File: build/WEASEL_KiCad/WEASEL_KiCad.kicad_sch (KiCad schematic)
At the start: 104 parts, among them J1 MIDI IN, J10 LPG_LEVEL2CTRL, J14 SEQ_OUTPUT2, J15 SEQ_OUTPUT3, J16 EG_OUTPUT1, J17 EG_OUTPUT2, J18 EG_OUTPUT3, J19 PLSR_OUTPUT1, J2 STEREO_OUTPUT, J20 PLSR_OUTPUT2, J21 PLSR_OUTPUT3, J22 RNDM_OUTPUT1, J23 RNDM_OUTPUT2, J24 RNDM_OUTPUT3, J3 SEQ_OUTPUT1, J4 PLSR_PERIODCTRL, J5 MODOSC_FREQCTRL, J6 MODOSC_MODCTRL, J7 COMPOSC_PITCHCTRL, J8 COMPOSC_WAVEFOLDERCTRL, J9 LPG_LEVEL1CTRL, SW1 SQ_TOGGLESTEP1, SW2 SEQ_TRIGGERSELECT, SW3 SQ_TOGGLESTEP2, SW31 EG_TRIGGERSELECT, SW32 EG_MODESELECT, SW33 PLSR_TRIGGERSELECT, SW34 PLSR_MODE, SW35 MODOSC_MIDITOGGLE, SW36 MODOSC_PITCHTRANGE, SW37 COMPLEXOSC_MIDITOGGLE, SW38 COMPLEXOSC_POLARITY, SW39 COMPLEXOSC_WAVETOGGLE, SW4 SQ_TOGGLESTEP3, SW40 LPG_GATE1MODE, SW41 LPG_GATE2MODE, SW42 RNDMVOLTAGE_TRIGGERSELECT, SW43 CLOCK_SYNCTOGGLE, SW5 SQ_TOGGLESTEP4, SW6 SEQ_STAGES, SW7 SQ_TOGGLESTEP5, U1 CD74HC4067, U2 CD74HC4067, U3 6N138

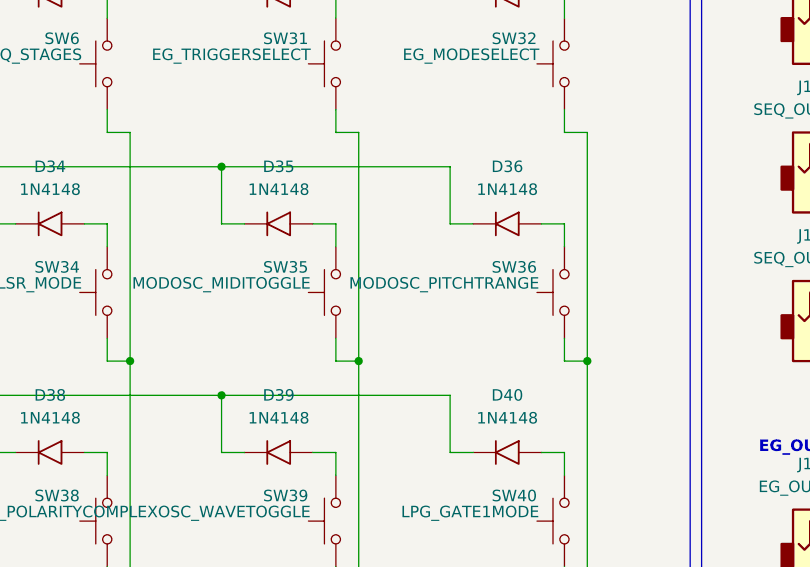
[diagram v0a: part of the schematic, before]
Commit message: FW update - prototype board
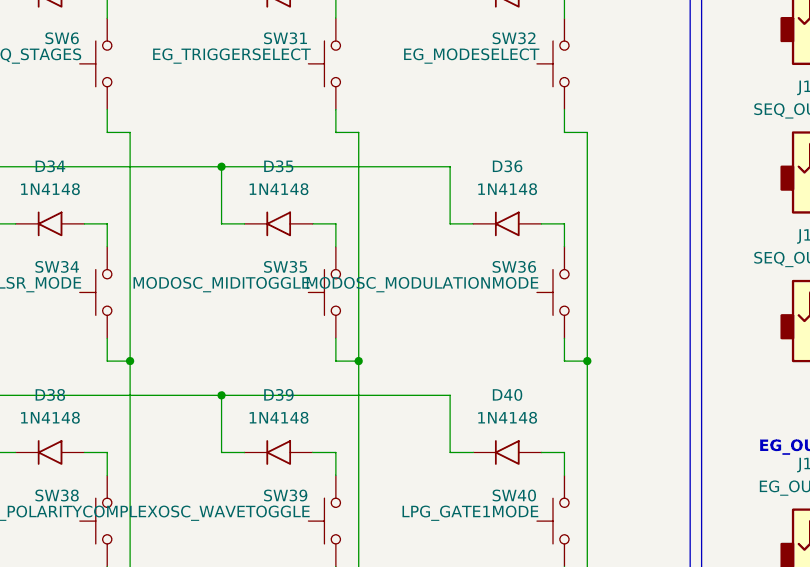
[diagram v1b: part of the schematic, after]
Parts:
- SW36: value MODOSC_PITCHTRANGE -> MODOSC_MODULATIONMODE
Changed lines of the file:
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@@
 			)
 		)
-		(property "Value" "MODOSC_PITCHTRANGE"
+		(property "Value" "MODOSC_MODULATIONMODE"
 			(at 138.176 211.074 90)
 			(effects

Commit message: PCB V2.0
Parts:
- J1, J2: footprint Connector_Audio:Jack_3.5mm_CUI_SJ1-3523N_Horizontal -> trsSocket:Jack_3.5mm_CUI_SJ1-3523N_Horizontal_edited_noEdgeCuts
- RV1, RV10, RV11, RV12, RV13, RV14, RV16, RV17, RV19, RV2, RV20, RV22, RV23, RV24, RV25, RV3, RV4, RV5, RV6, RV7, RV8, RV9: footprint DIYSynthMNL:Potentiometer_RV09_BigPads -> Potentiometer_THT:Potentiometer_Bourns_PTA2043_Single_Slide
- U1, U2: footprint CD74HC4067 MUX:CD74HC4067 -> CD74HC4067 MUX:CD74HC4067_matchesSymbol
- renumbered D44 to D1, D36 to D10, D37 to D11, D38 to D12, D39 to D13, D40 to D14, D41 to D15, D42 to D16, D43 to D17, D45 to D18, D46 to D19, D47 to D20, D48 to D21, D49 to D22, D1 to D23, D2 to D24, D3 to D25, D4 to D26, D6 to D27, D7 to D28, D8 to D29, D5 to D3, D30 to D4, D31 to D5, D32 to D6, D33 to D7, D34 to D8, D35 to D9, J20 to J10, J21 to J11, J22 to J12, J23 to J13, J24 to J14, J4 to J15, J5 to J16, J6 to J17, J7 to J18, J8 to J19, J9 to J20, J10 to J21, J14 to J4, J15 to J5, J16 to J6, J17 to J7, J18 to J8, J19 to J9, R10 to R1, R9 to R2, SW2 to SW1, SW38 to SW10, SW39 to SW11, SW40 to SW12, SW41 to SW13, SW42 to SW14, SW43 to SW15, SW1 to SW16, SW3 to SW17, SW4 to SW18, SW5 to SW19, SW6 to SW2, SW7 to SW20, SW31 to SW3, SW32 to SW4, SW33 to SW5, SW34 to SW6, SW35 to SW7, SW36 to SW8, SW37 to SW9
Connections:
- net GND: now also RV12.1; no longer A1.20 (AGND), J2.S, RV12.3
- net Vcc: now also RV12.3; no longer RV12.1
- new net AGND: A1.20 (AGND), J2.S
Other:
- moved on the sheet: RV12

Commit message: PCB & UI 2.0
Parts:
- SW7: value MODOSC_MIDITOGGLE -> MODOSC_WAVEFORMTOGGLE
- SW9: value COMPLEXOSC_MIDITOGGLE -> OSCILLATOR_MIDITOGGLE
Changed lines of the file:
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@@
 			)
 		)
-		(property "Value" "MODOSC_MIDITOGGLE"
+		(property "Value" "MODOSC_WAVEFORMTOGGLE"
 			(at 112.776 211.074 90)
 			(effects
@@
 			)
 		)
-		(property "Value" "COMPLEXOSC_MIDITOGGLE"
+		(property "Value" "OSCILLATOR_MIDITOGGLE"
 			(at 61.468 236.982 90)
 			(effects

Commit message: PCB & UI 2.0
Front Panel final
Back panel Final
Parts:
- SW7: value MODOSC_WAVEFORMTOGGLE -> MODOSC_MODULATIONMODE
- SW8: value MODOSC_MODULATIONMODE -> MODOSC_WAVEFORMTOGGLE
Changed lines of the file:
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@@
 			)
 		)
-		(property "Value" "MODOSC_WAVEFORMTOGGLE"
-			(at 112.776 211.074 90)
+		(property "Value" "MODOSC_MODULATIONMODE"
+			(at 119.126 216.408 90)
 			(effects
 				(font
@@
 			)
 		)
-		(property "Value" "MODOSC_MODULATIONMODE"
-			(at 138.176 211.074 90)
+		(property "Value" "MODOSC_WAVEFORMTOGGLE"
+			(at 142.24 207.772 90)
 			(effects
 				(font

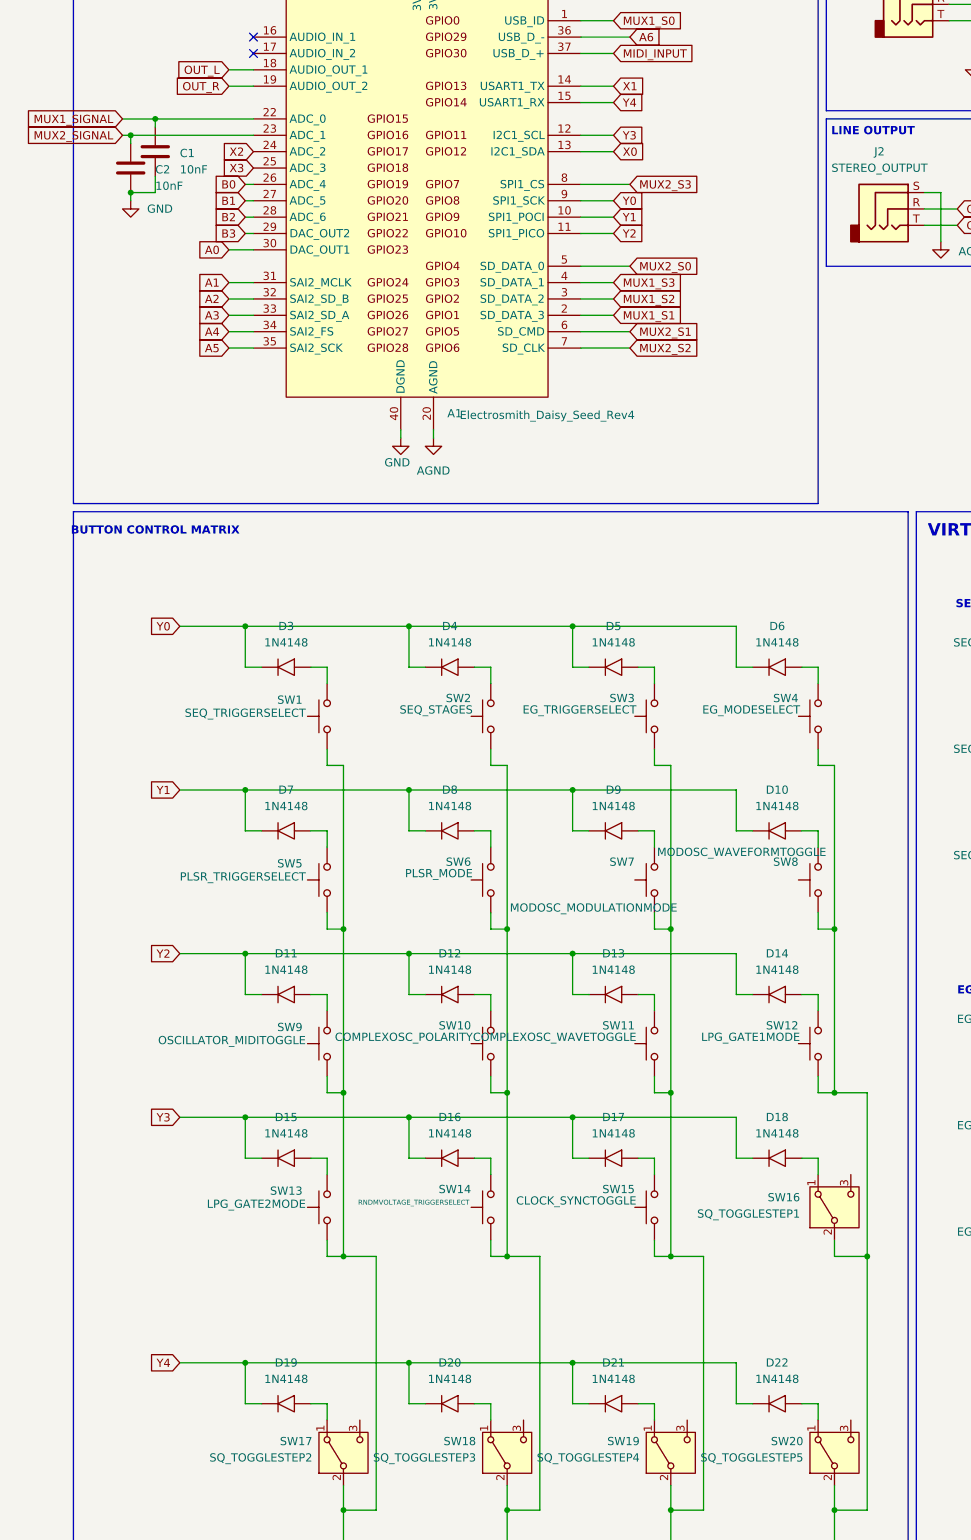
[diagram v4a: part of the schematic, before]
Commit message: PCB and Firmware Updates
- Updated PCBs
- Updated firmware to add sequencer trigger toggle - sequencer can now be triggered by pulser. Midi is WIP
- Updated Pot names in Serial
- Fixed X1 Row button issues
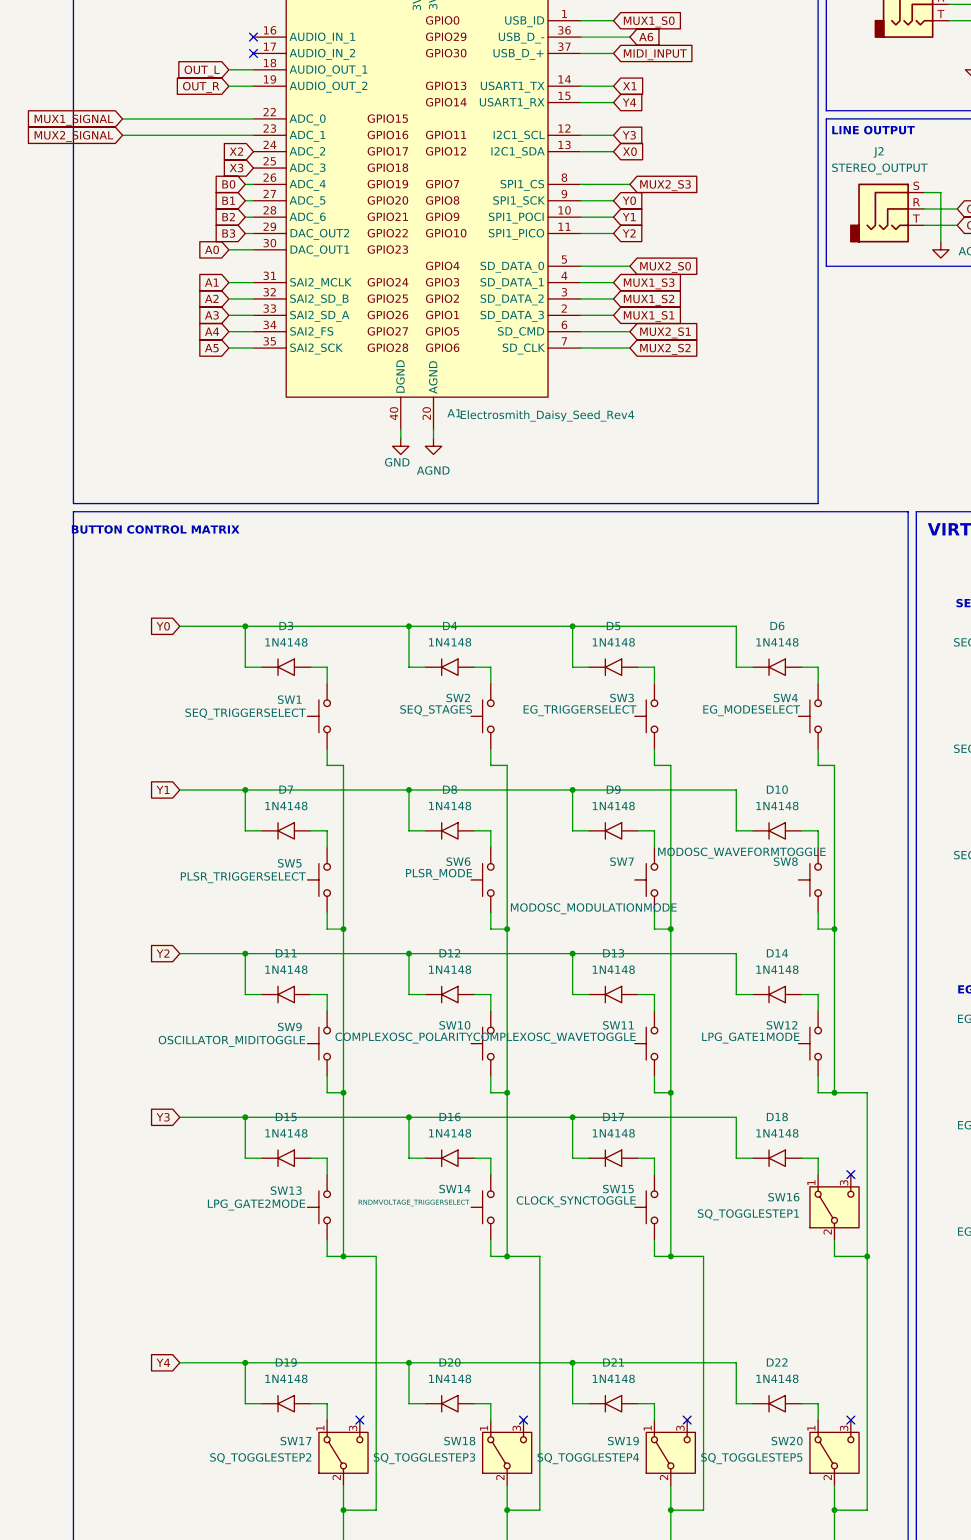
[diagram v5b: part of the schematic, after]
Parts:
- removed C1, C2: 10nF, PCM_4ms_Capacitor:C_Disc_P5.08mm, symbol Device:C
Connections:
- no-connect marks 9 -> 14

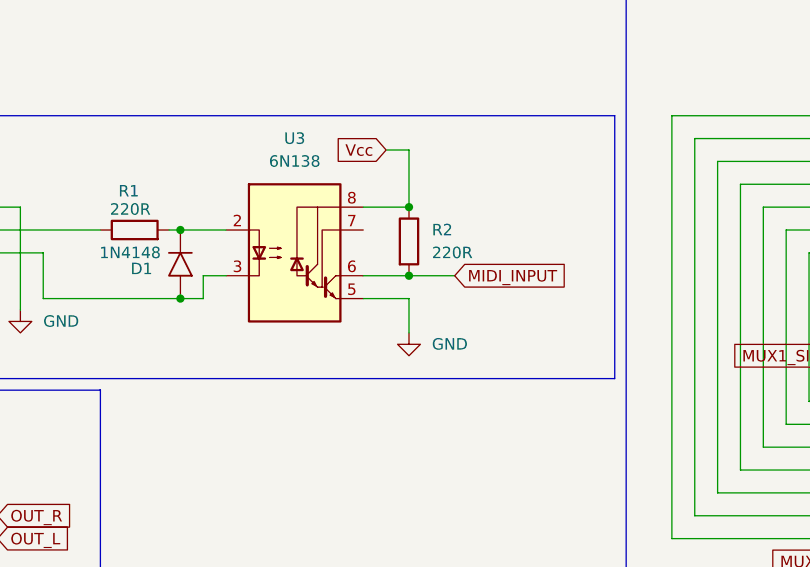
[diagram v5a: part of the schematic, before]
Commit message: Smoothed POTS
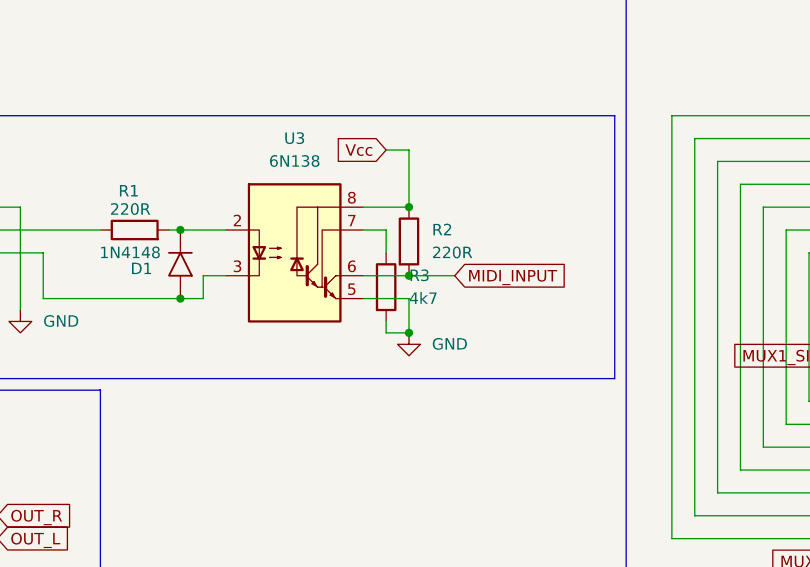
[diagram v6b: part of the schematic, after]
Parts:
- added R3: 4k7, PCM_4ms_Resistor:R_Axial_DIN0207_L6.3mm_D2.5mm_P7.62mm_Horizontal, symbol Device:R
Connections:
- net GND: now also R3.2
- net at U3.7 (VO1): now also R3.1
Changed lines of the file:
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@@
 	)
 	(junction
+		(at 208.28 87.63)
+		(diameter 0)
+		(color 0 0 0 0)
+	)
+	(junction
 		(at 205.74 270.51)
 		(diameter 0)
@@
 	(wire
 		(pts
+			(xy 205.74 87.63) (xy 208.28 87.63)
+		)
+		(stroke
+			(width 0)
+			(type default)
+		)
+	)
+	(wire
+		(pts
 			(xy 568.96 172.72) (xy 568.96 198.12)
 		)
@@
 	(wire
 		(pts
+			(xy 205.74 76.2) (xy 203.2 76.2)
+		)
+		(stroke
+			(width 0)
+			(type default)
+		)
+	)
+	(wire
+		(pts
 			(xy 238.76 179.07) (xy 246.38 179.07)
 		)
@@
 	(wire
 		(pts
+			(xy 205.74 78.74) (xy 205.74 76.2)
+		)
+		(stroke
+			(width 0)
+			(type default)
+		)
+	)
+	(wire
+		(pts
 			(xy 238.76 207.01) (xy 238.76 209.55)
 		)
@@
 	(wire
 		(pts
+			(xy 205.74 86.36) (xy 205.74 87.63)
+		)
+		(stroke
+			(width 0)
+			(type default)
+		)
+	)
+	(wire
+		(pts
 			(xy 321.31 101.6) (xy 706.12 101.6)
 		)
@@
 					(unit 1)
 				)
+			)
+		)
+	)
+	(symbol
+		(lib_id "Device:R")
+		(at 205.74 82.55 0)
+		(unit 1)
+		(exclude_from_sim no)
+		(in_bom yes)
+		(on_board yes)
+		(dnp no)
+		(property "Reference" "R3"
+			(at 208.28 81.2799 0)
+			(effects
+				(font
+					(size 1.27 1.27)
+				)
+				(justify left)
+			)
+		)
+		(property "Value" "4k7"
+			(at 208.28 83.8199 0)
+			(effects
+				(font
+					(size 1.27 1.27)
+				)
+				(justify left)
+			)
+		)
+		(property "Footprint" "PCM_4ms_Resistor:R_Axial_DIN0207_L6.3mm_D2.5mm_P7.62mm_Horizontal"
+			(at 203.962 82.55 90)
+			(effects
+				(font
+					(size 1.27 1.27)
+				)
+				(hide yes)
+			)
+		)
+		(property "Datasheet" "~"
+			(at 205.74 82.55 0)
+			(effects
+				(font
+					(size 1.27 1.27)
+				)
+				(hide yes)
+			)
+		)
+		(property "Description" "Resistor"
+			(at 205.74 82.55 0)
+			(effects
+				(font
+					(size 1.27 1.27)
+				)
+				(hide yes)
+			)
+		)
+		(pin "1"
+		)
+		(pin "2"
+		)
+		(instances
+			(project "WEASEL_KiCad"
+				(path "/3720ecea-634e-451d-a5f4-988a924d60a3"
+					(reference "R3")
+					(unit 1)
+				)

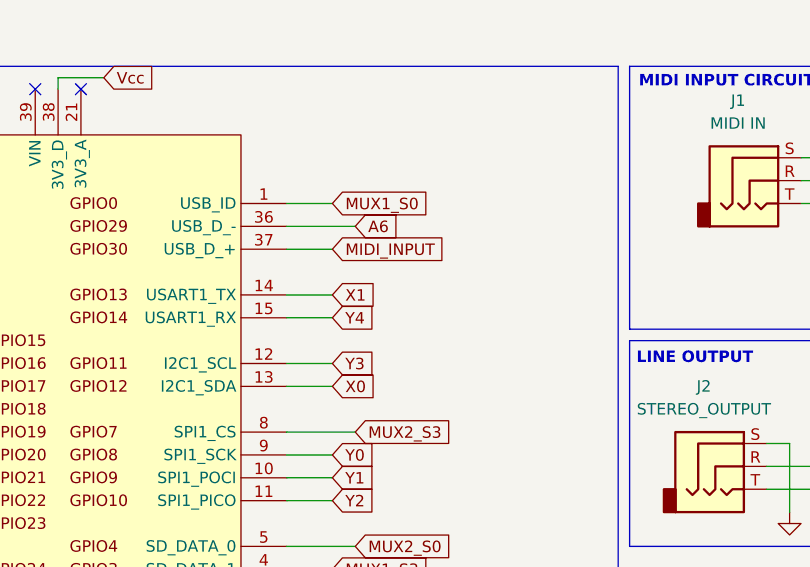
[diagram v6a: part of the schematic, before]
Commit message: MIDI IN pots change
Swapped Y4 and RX pins
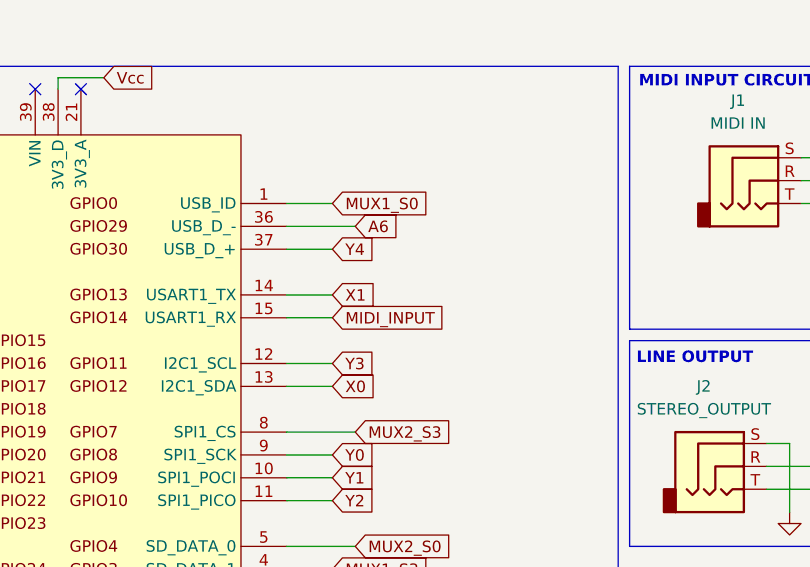
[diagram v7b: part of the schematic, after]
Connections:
- net MIDI_INPUT: now also A1.15 (USART1_RX); no longer A1.37 (USB_D_+)
- net Y4: now also A1.37 (USB_D_+); no longer A1.15 (USART1_RX)

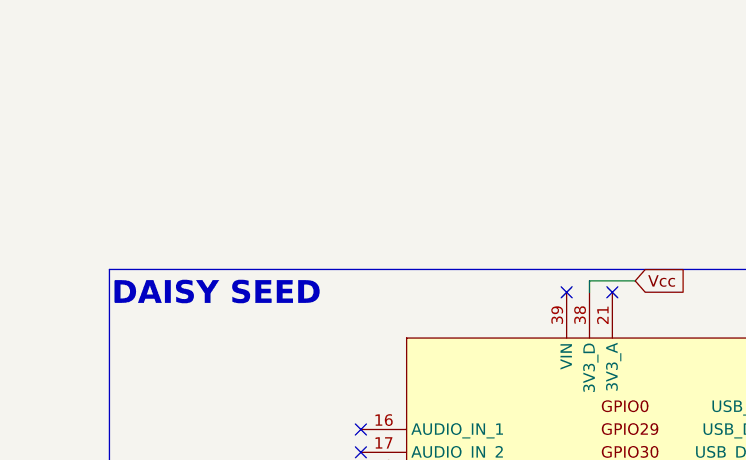
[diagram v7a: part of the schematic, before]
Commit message: PCB Update
Added  5V Power Input
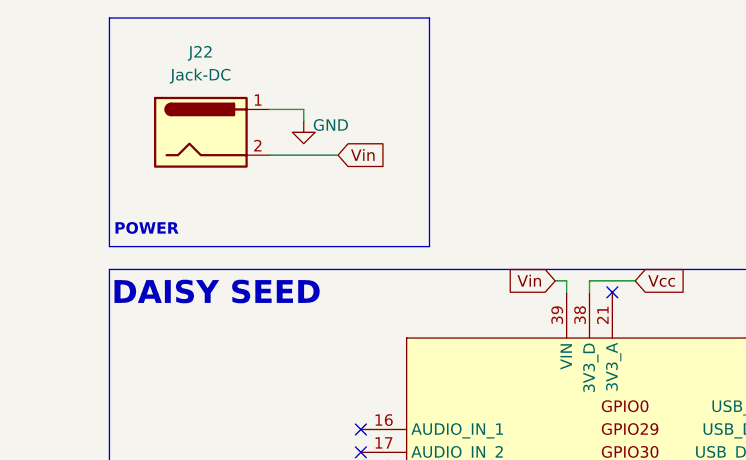
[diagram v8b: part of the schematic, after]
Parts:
- added J22: Jack-DC, Connector_BarrelJack:BarrelJack_GCT_DCJ200-10-A_Horizontal, symbol Connector:Jack-DC
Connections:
- net GND: now also J22.1
- net Vin: now reaches A1.39 (VIN)
- net Vin: now also J22.2
- no-connect marks 14 -> 13
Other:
- note added: "POWER"
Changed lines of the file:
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@@
 	)
 	(rectangle
+		(start 25.4 35.56)
+		(end 60.96 60.96)
+		(stroke
+			(width 0)
+			(type default)
+		)
+		(fill
+			(type none)
+		)
+	)
+	(rectangle
 		(start 142.24 93.98)
 		(end 173.99 116.84)
@@
 		)
 	)
+	(text "POWER"
+		(exclude_from_sim no)
+		(at 25.908 59.182 0)
+		(effects
+			(font
+				(size 1.27 1.27)
+				(thickness 0.254)
+				(bold yes)
+			)
+			(justify left)
+		)
+	)
 	(text "PLSR_PERIODCTRL"
 		(exclude_from_sim no)
@@
 	)
 	(no_connect
-		(at 76.2 66.04)
-	)
-	(no_connect
 		(at 53.34 81.28)
 	)
@@
 	(wire
 		(pts
+			(xy 74.93 64.77) (xy 76.2 64.77)
+		)
+		(stroke
+			(width 0)
+			(type default)
+		)
+	)
+	(wire
+		(pts
 			(xy 247.65 73.66) (xy 247.65 100.33)
 		)
@@
 	(wire
 		(pts
+			(xy 46.99 46.99) (xy 46.99 45.72)
+		)
+		(stroke
+			(width 0)
+			(type default)
+		)
+	)
+	(wire
+		(pts
 			(xy 359.41 168.91) (xy 361.95 168.91)
 		)
@@
 	(wire
 		(pts
+			(xy 43.18 50.8) (xy 50.8 50.8)
+		)
+		(stroke
+			(width 0)
+			(type default)
+		)
+	)
+	(wire
+		(pts
 			(xy 87.63 204.47) (xy 90.17 204.47)
 		)
@@
 	(wire
 		(pts
+			(xy 76.2 64.77) (xy 76.2 66.04)
+		)
+		(stroke
+			(width 0)
+			(type default)
+		)
+	)
+	(wire
+		(pts
 			(xy 629.92 168.91) (xy 629.92 176.53)
 		)
@@
 	(wire
 		(pts
+			(xy 46.99 45.72) (xy 43.18 45.72)
+		)
+		(stroke
+			(width 0)
+			(type default)
+		)
+	)
+	(wire
+		(pts
 			(xy 41.91 287.02) (xy 52.07 287.02)
 		)
@@
 		)
 	)
+	(global_label "Vin"
+		(shape input)
+		(at 74.93 64.77 180)
+		(fields_autoplaced yes)
+		(effects
+			(font
+				(size 1.27 1.27)
+			)
+			(justify right)
+		)
+		(property "Intersheetrefs" "${INTERSHEET_REFS}"
+			(at 69.1024 64.77 0)
+			(effects
+				(font
+					(size 1.27 1.27)
+				)
+				(justify right)
+				(hide yes)
+			)
+		)
+	)
 	(global_label "MUX2_SIGNAL"
 		(shape input)
@@
 		)
 	)
+	(global_label "Vin"
+		(shape input)
+		(at 50.8 50.8 0)
+		(fields_autoplaced yes)
+		(effects
+			(font
+				(size 1.27 1.27)
+			)
+			(justify left)
+		)
+		(property "Intersheetrefs" "${INTERSHEET_REFS}"
+			(at 56.6276 50.8 0)
+			(effects
+				(font
+					(size 1.27 1.27)
+				)
+				(justify left)
+				(hide yes)
+			)
+		)
+	)
 	(global_label "Vcc"
 		(shape input)
@@
 	)
 	(symbol
+		(lib_id "Connector:Jack-DC")
+		(at 35.56 48.26 0)
+		(unit 1)
+		(exclude_from_sim no)
+		(in_bom yes)
+		(on_board yes)
+		(dnp no)
+		(fields_autoplaced yes)
+		(property "Reference" "J22"
+			(at 35.56 39.37 0)
+			(effects
+				(font
+					(size 1.27 1.27)
+				)
+			)
+		)
+		(property "Value" "Jack-DC"
+			(at 35.56 41.91 0)
+			(effects
+				(font
+					(size 1.27 1.27)
+				)
+			)
+		)
+		(property "Footprint" "Connector_BarrelJack:BarrelJack_GCT_DCJ200-10-A_Horizontal"
+			(at 36.83 49.276 0)
+			(effects
+				(font
+					(size 1.27 1.27)
+				)
+				(hide yes)
+			)
+		)
+		(property "Datasheet" "~"
+			(at 36.83 49.276 0)
+			(effects
+				(font
+					(size 1.27 1.27)
+				)
+				(hide yes)
+			)
+		)
+		(property "Description" "DC Barrel Jack"
+			(at 35.56 48.26 0)
+			(effects
+				(font
+					(size 1.27 1.27)
+				)
+				(hide yes)
+			)
+		)
+		(pin "2"
+		)
+		(pin "1"
+		)
+		(instances
+			(project ""
+				(path "/3720ecea-634e-451d-a5f4-988a924d60a3"
+					(reference "J22")
+					(unit 1)
+				)
+			)
+		)
+	)
+	(symbol
 		(lib_id "power:GND")
 		(at 160.02 113.03 0)
@@
 					(unit 1)
 				)
+			)
+		)
+	)
+	(symbol
+		(lib_id "power:GND")
+		(at 46.99 46.99 0)
+		(unit 1)
+		(exclude_from_sim no)
+		(in_bom yes)
+		(on_board yes)
+		(dnp no)
+		(property "Reference" "#PWR01"
+			(at 46.99 53.34 0)
+			(effects
+				(font
+					(size 1.27 1.27)
+				)
+				(hide yes)
+			)
+		)
+		(property "Value" "GND"
+			(at 48.006 47.498 0)
+			(effects
+				(font
+					(size 1.27 1.27)
+				)
+				(justify left)
+			)
+		)
+		(property "Footprint" ""
+			(at 46.99 46.99 0)
+			(effects
+				(font
+					(size 1.27 1.27)
+				)
+				(hide yes)
+			)
+		)
+		(property "Datasheet" ""
+			(at 46.99 46.99 0)
+			(effects
+				(font
+					(size 1.27 1.27)
+				)
+				(hide yes)
+			)
+		)
+		(property "Description" "Power symbol creates a global label with name \"GND\" , ground"
+			(at 46.99 46.99 0)
+			(effects
+				(font
+					(size 1.27 1.27)
+				)
+				(hide yes)
+			)
+		)
+		(pin "1"
+		)
+		(instances
+			(project "WEASEL_KiCad"
+				(path "/3720ecea-634e-451d-a5f4-988a924d60a3"
+					(reference "#PWR01")
+					(unit 1)
+				)
